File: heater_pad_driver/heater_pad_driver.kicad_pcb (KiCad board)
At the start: 2 copper layers, 55 x 45 mm, 25 parts, among them J1 24V_IN, J2 GND_IN, J3 Heater_Conn, J4 CTL_Conn, Q1 NPN, Q2 NMOS, U1 UCC23525CDWYR, U2 ACS713xLCTR-30A

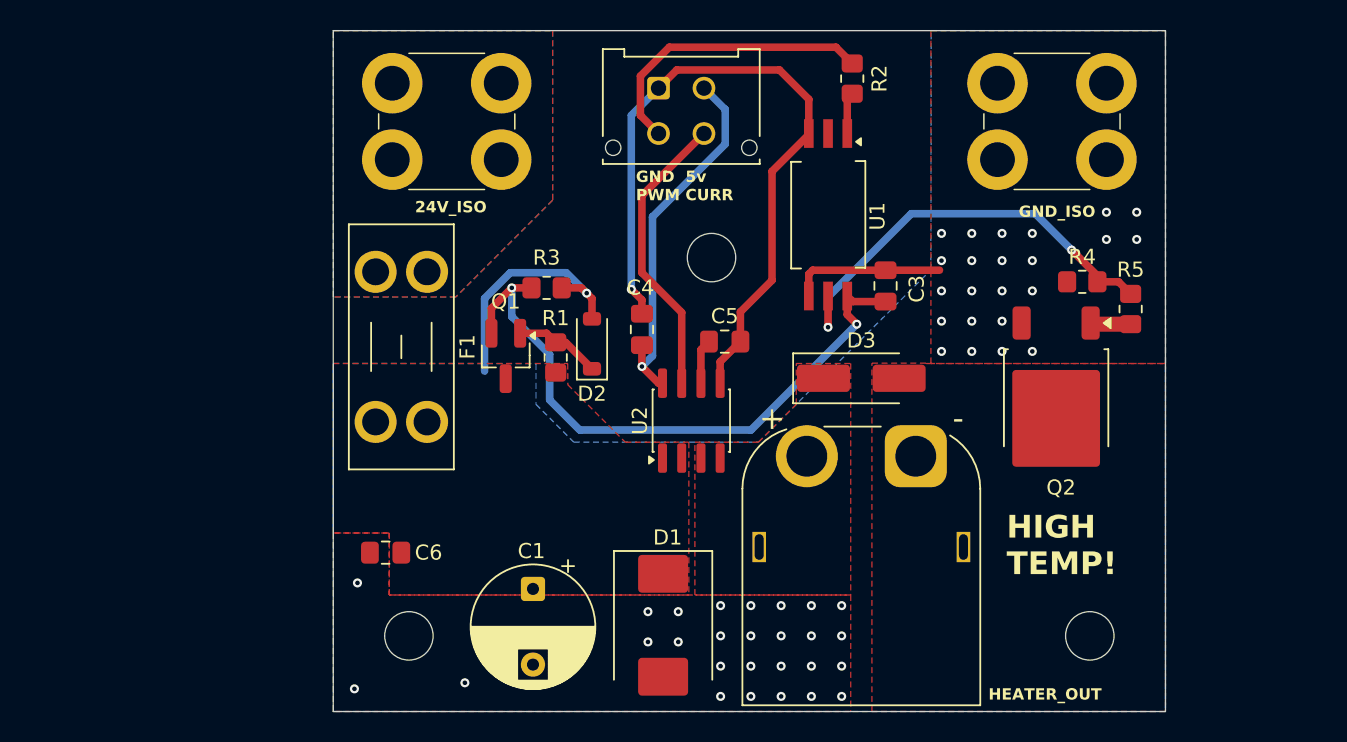
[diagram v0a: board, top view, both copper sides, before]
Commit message: add relay to heater board for estop and do some ignitor board routing
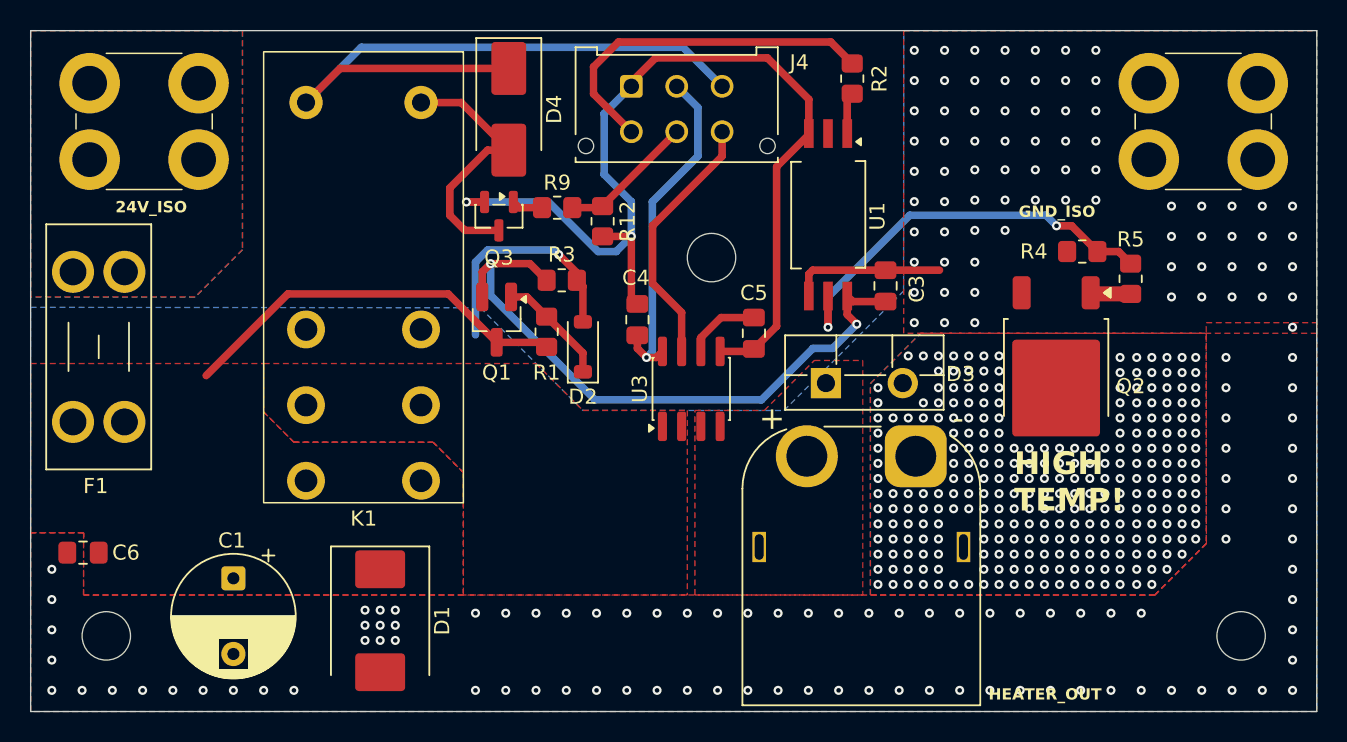
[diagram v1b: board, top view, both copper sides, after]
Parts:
- removed U2: ACS713xLCTR-30A, Package_SO:SOIC-8_3.9x4.9mm_P1.27mm
- added D4: SK44BL, Diode_SMD:D_SMB_Handsoldering, F.Cu at (107.1, 72.7)
- added K1: Relay_SPDT, Library:AZ576-1C, F.Cu at (97.5, 83.8)
- added Q3: BSS138, Package_TO_SOT_SMD:SOT-23, F.Cu at (106.5, 79.8)
- added R12: 100k, Resistor_SMD:R_0805_2012Metric_Pad1.20x1.40mm_HandSolder, F.Cu at (113.3, 80.1)
- added R9: 100, Resistor_SMD:R_0805_2012Metric_Pad1.20x1.40mm_HandSolder, F.Cu at (110.3, 79.2)
- added U3: ACS713xLCTR-20A, Package_SO:SOIC-8_3.9x4.9mm_P1.27mm, F.Cu at (119.2, 91.2)
- D3: value 100V -> Flyback; footprint Diode_SMD:D_SMA_Handsoldering -> Package_TO_SOT_THT:TO-220F-2_Vertical
- J4: footprint Connector_Molex:Molex_Micro-Fit_3.0_43045-0412_2x02_P3.00mm_Vertical -> Connector_Molex:Molex_Micro-Fit_3.0_43045-0612_2x03_P3.00mm_Vertical
- R1: value 680 -> 1k
- R4: value 100k -> 10k
- moved C6 20.0 mm to (79.0, 102.0)
- moved F1 20.0 mm to (81.7, 83.4)
- moved H3 20.0 mm to (80.5, 107.5)
- moved J1 20.0 mm to (83.0, 73.5)
- moved C1 19.8 mm to (88.9, 103.7)
- moved D1 18.7 mm to (98.6, 106.5)
- moved H1 10.0 mm to (155.5, 107.5)
- moved J2 10.0 mm to (153.0, 73.5)
- moved Q1 2.47 mm to (106.3, 86.6)
- moved D3 2.36 mm to (128.1, 90.8)
- moved C5 2.01 mm to (123.3, 87.5), turned to -90 degrees
- moved Q2 2.00 mm to (143.3, 89.9)
- moved R4 2.00 mm to (145.0, 82.1)
- moved R5 2.00 mm to (148.2, 83.9)
- moved J4 1.80 mm to (115.2, 71.2)
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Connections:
- J4 pad 3: /PWM_CONN -> /24V_CONN
- J4 pad 4: /CURR_CONN -> /PWM_CONN
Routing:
- net /24V_CONN: track 0.00 -> 44.4 mm
- net +24V_ISO: track 0.00 -> 26.2 mm
- net /GND_CONN: track 48.4 -> 65.9 mm, vias 1 -> 2
- net Net-(D4-A): track 0.00 -> 17.5 mm
- net /ESTOP_CONN: track 0.00 -> 8.99 mm
- net /PWM_CONN: track 19.5 -> 23.7 mm
- net /CURR_CONN: track 19.3 -> 17.2 mm
- net Net-(Q3-G): track 0.00 -> 2.06 mm
- net Net-(U3-FILTER): track 2.97 -> 4.96 mm
- net /5V_CONN: track 24.5 -> 22.8 mm
- net Net-(D2-K): track 5.94 -> 7.53 mm
- net Net-(U1-VO): track 28.8 -> 27.6 mm
- net GND_ISO: track 26.6 -> 26.1 mm, vias 51 -> 168
- net Net-(D3-A): vias 0 -> 269
- added copper zone on B.Cu, net Net-(D3-A)
- added copper zone on F.Cu, net Net-(K1-Pad11)
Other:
- board size 55 x 45 mm -> 85 x 45 mm
- board text added: "24V 5v GND CURR ESTOP PWM"
- board text removed: "GND 5v PWM CURR"

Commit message: updates for manufacturing
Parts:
- D4: value SK44BL -> SK44BL-TP
- U3: value ACS713xLCTR-20A -> ACS724xLCTR-30AU
- moved D3 0.38 mm to (127.8, 90.5)
- moved C4 0.20 mm to (115.4, 86.6)
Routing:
- net Net-(D3-A): vias 269 -> 265
